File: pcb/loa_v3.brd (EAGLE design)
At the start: 50.9 x 81.4 mm, 111 parts, among them IC1 STM32F10XVXT6, IC2 M25P80MW, IC3 S34ML04G100TFI000, IC4 MCP1825S-1202E/DB, IC5 NCP3170, IC6 AD7265SU, Q2 50.000, Q3 25.000, U1 6SLX9TQG144, X3 MINI-USB

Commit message: Fixed DP and DM naming for USB
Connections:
- net USB_D+: now also JP3.3, R13.2, X3.3; no longer JP3.2, R12.2, X3.2
- net USB_D-: now also JP3.2, R12.2, X3.2; no longer JP3.3, R13.2, X3.3
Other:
- board text added: "1"
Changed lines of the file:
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@@
 <?xml version="1.0" encoding="utf-8"?>
 <!DOCTYPE eagle SYSTEM "eagle.dtd">
-<eagle version="6.5.0">
+<eagle version="6.4">
 <drawing>
 <settings>
@@
 <wire x1="26.3525" y1="-3.7625" x2="25.3525" y2="-4.7625" width="0.4064" layer="49" curve="-90"/>
 <wire x1="18.4625" y1="-4.7625" x2="17.4625" y2="-3.7625" width="0.4064" layer="49" curve="-90"/>
-<wire x1="5.08" y1="38.1" x2="35.0837" y2="38.1" width="0.254" layer="47"/>
-<wire x1="40.1638" y1="40.1638" x2="35.0838" y2="40.1638" width="0.254" layer="47"/>
 <wire x1="18.4625" y1="-1.1113" x2="17.4625" y2="-0.1113" width="0.4064" layer="49" curve="-90"/>
 <wire x1="26.3525" y1="-0.1113" x2="25.3525" y2="-1.1113" width="0.4064" layer="49" curve="-90"/>
@@
 <wire x1="13.0175" y1="75.40625" x2="13.81125" y2="75.40625" width="0.1" layer="25"/>
 <wire x1="13.81125" y1="75.40625" x2="14.12875" y2="75.08875" width="0.1" layer="25"/>
+<dimension x1="1.27" y1="1.27" x2="46.99" y2="1.27" x3="24.13" y3="-10.16" textsize="1.778" layer="47"/>
+<dimension x1="3.81" y1="1.27" x2="3.81" y2="11.43" x3="17.145" y3="6.35" textsize="1.778" layer="47"/>
+<dimension x1="0" y1="0" x2="50.9388" y2="0" x3="25.4694" y3="-15.875" textsize="1.778" layer="47"/>
+<dimension x1="50.9388" y1="0" x2="50.9388" y2="81.4263" x3="58.42" y3="40.71315" textsize="1.778" layer="47"/>
+<dimension x1="1.27" y1="80.01" x2="21.59" y2="80.01" x3="11.43" y3="93.98" textsize="1.778" layer="47"/>
+<dimension x1="1.27" y1="80.01" x2="13.97" y2="80.01" x3="7.62" y3="88.265" textsize="1.778" layer="47"/>
+<dimension x1="1.27" y1="1.27" x2="29.21" y2="1.27" x3="15.24" y3="-5.08" textsize="1.778" layer="47"/>
+<dimension x1="39.37" y1="3.81" x2="39.37" y2="1.27" x3="45.085" y3="2.54" textsize="1.778" layer="47"/>
+<dimension x1="1.27" y1="1.27" x2="1.27" y2="74.93" x3="19.685" y3="38.1" textsize="1.778" layer="47"/>
+<text x="-1.905" y="79.375" size="1.778" layer="47">1</text>
+<text x="44.45" y="79.375" size="1.778" layer="47">1</text>
+<text x="8.255" y="15.875" size="1.778" layer="47">1</text>
 </plain>
 <attributes>
@@
 <wire x1="15.77255" y1="10.6363" x2="15.875" y2="10.6363" width="0.3048" layer="1"/>
 </signal>
-<signal name="USB_D-">
+<signal name="USB_D+">
 <contactref element="X3" pad="3"/>
 <contactref element="R13" pad="2"/>
@@
 <wire x1="14.0725" y1="10.63625" x2="14.07255" y2="10.6363" width="0.3048" layer="1"/>
 </signal>
-<signal name="USB_D+">
+<signal name="USB_D-">
 <contactref element="X3" pad="2"/>
 <contactref element="R12" pad="2"/>
@@
 </signal>
 </signals>
-<errors>
-</errors>
 </board>
 </drawing>

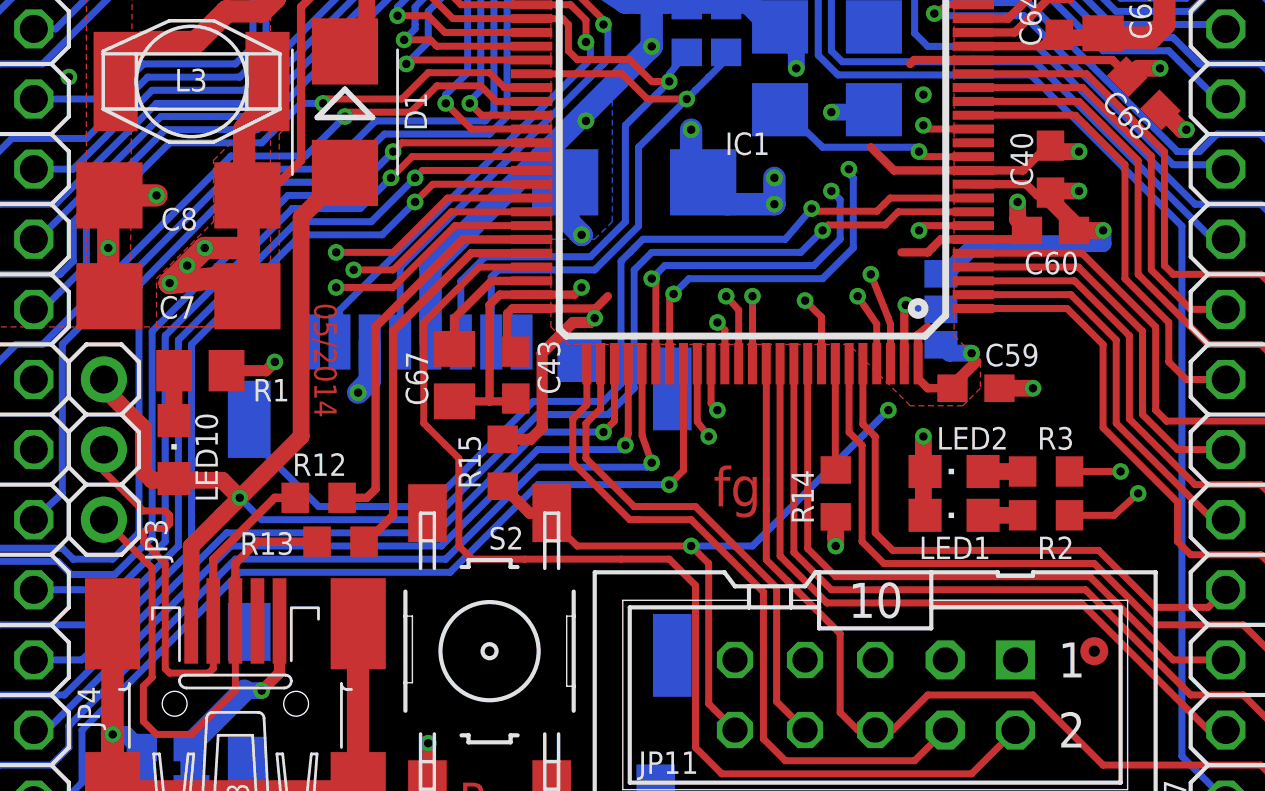
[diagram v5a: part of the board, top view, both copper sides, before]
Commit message: Voltage divider added for the V_USB sense pin
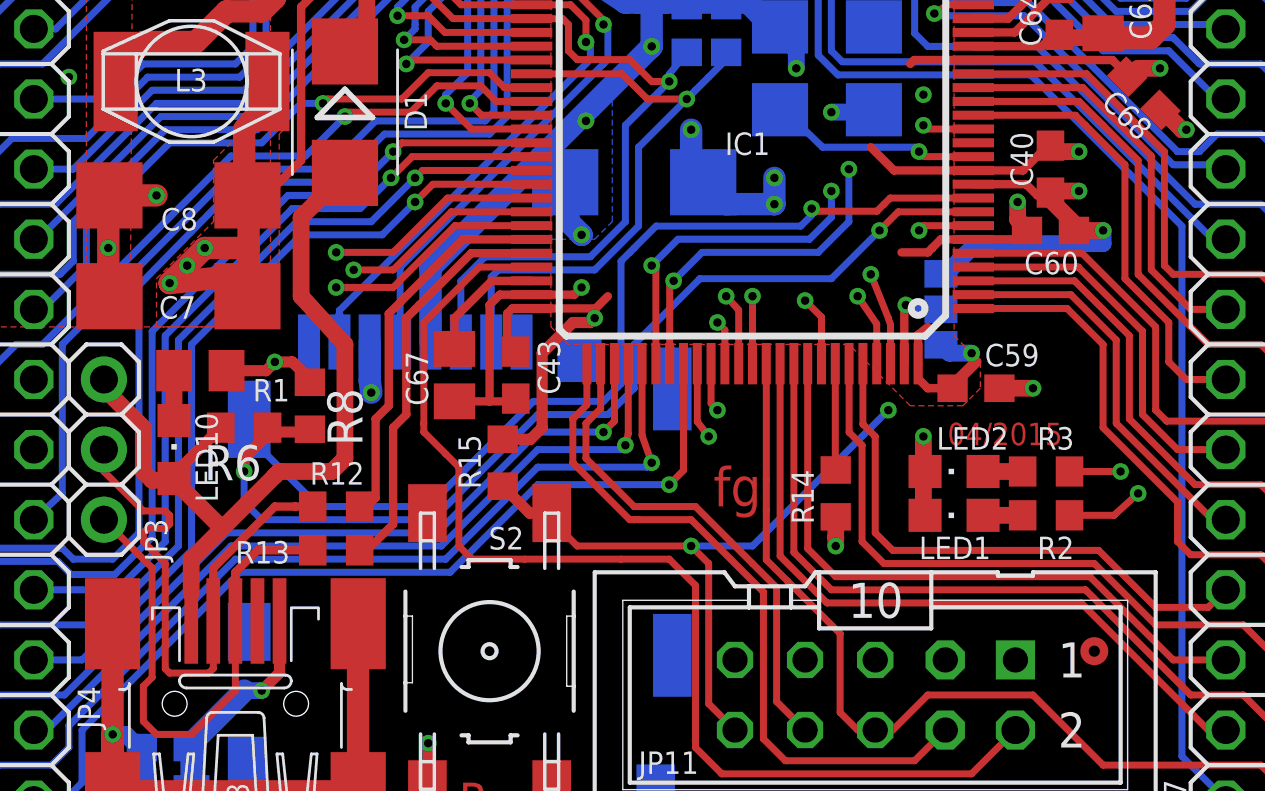
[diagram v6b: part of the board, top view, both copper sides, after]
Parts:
- added R6: 1k, rcl:R0603
- added R8: 2k2, rcl:R0603
- R15: value 10k -> 2k2
- moved R12 0.71 mm to (14.8, 11.9)
- moved R13 0.35 mm to (14.8, 10.3)
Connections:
- new net N$19: IC1.8, R6.1, R8.2
- net GND: now also R8.1
- net USB_VBUS: now also R6.2; no longer IC1.8
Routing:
- net N$19: track 0.00 -> 36.9 mm, vias 0 -> 2
- net USB_VBUS: track 62.4 -> 32.3 mm, vias 2 -> 0
- net GND: track 248.7 -> 250.1 mm
- net FSMC_D2: track 31.6 -> 31.0 mm
- net FSMC_D3: track 34.7 -> 34.2 mm
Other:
- board text added: "04/2015"
- board text removed: "05/2014"
